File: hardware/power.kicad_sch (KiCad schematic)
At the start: 42 parts, among them J15 Conn_01x02, Q13 DMP3013SFV, Q14 BC817W, U10 FP6151XR-G1, U8 ZTP7193MA

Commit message: clean up
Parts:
- removed Q14: BC817W, Package_TO_SOT_SMD:SOT-323_SC-70, symbol Transistor_BJT:BC817W
- added Q12: AO3400A, Package_TO_SOT_SMD:SOT-23, symbol Transistor_FET:AO3400A
- D3: renamed from D4; LCSC (none) -> C19077535
- renumbered C27 to C14, C36 to C15, C29 to C16, C31 to C17, C37 to C18, C38 to C19, C39 to C20, C33 to C21, C40 to C22, C35 to C23, C41 to C24, D3 to D4, J15 to J14, L3 to L1, Q13 to Q11, R40 to R26, R56 to R27, R44 to R28, R45 to R29, R46 to R30, R57 to R31, R58 to R32, R48 to R33, R59 to R34, R60 to R35, R51 to R36, R52 to R37, R53 to R38, R54 to R39, R55 to R40, TP7 to TP5, U8 to U5, U10 to U6
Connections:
- net GND: now also Q12.2 (S)
- net at R38.2, R39.1: now also Q12.1 (G)
- net at LED1.1 (K): now also Q12.3 (D)
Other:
- note added: "Need to set EN to be >6V"
- note added: "Power Supplies"
- note added: "Reverse Voltage Protection Q11 body diode blocks reverse polarity D2 will clamp V_{GS} to +10V"
- note removed: "Filtering Over Voltage Reverse Voltage"
- note removed: "Make input PMOS larger and include soft start Include large bulk cap for LEDs"
- note removed: "Reverse Voltage Protection Q1 body diode blocks reverse polarity D1 will clamp V_{GS} to +10V"

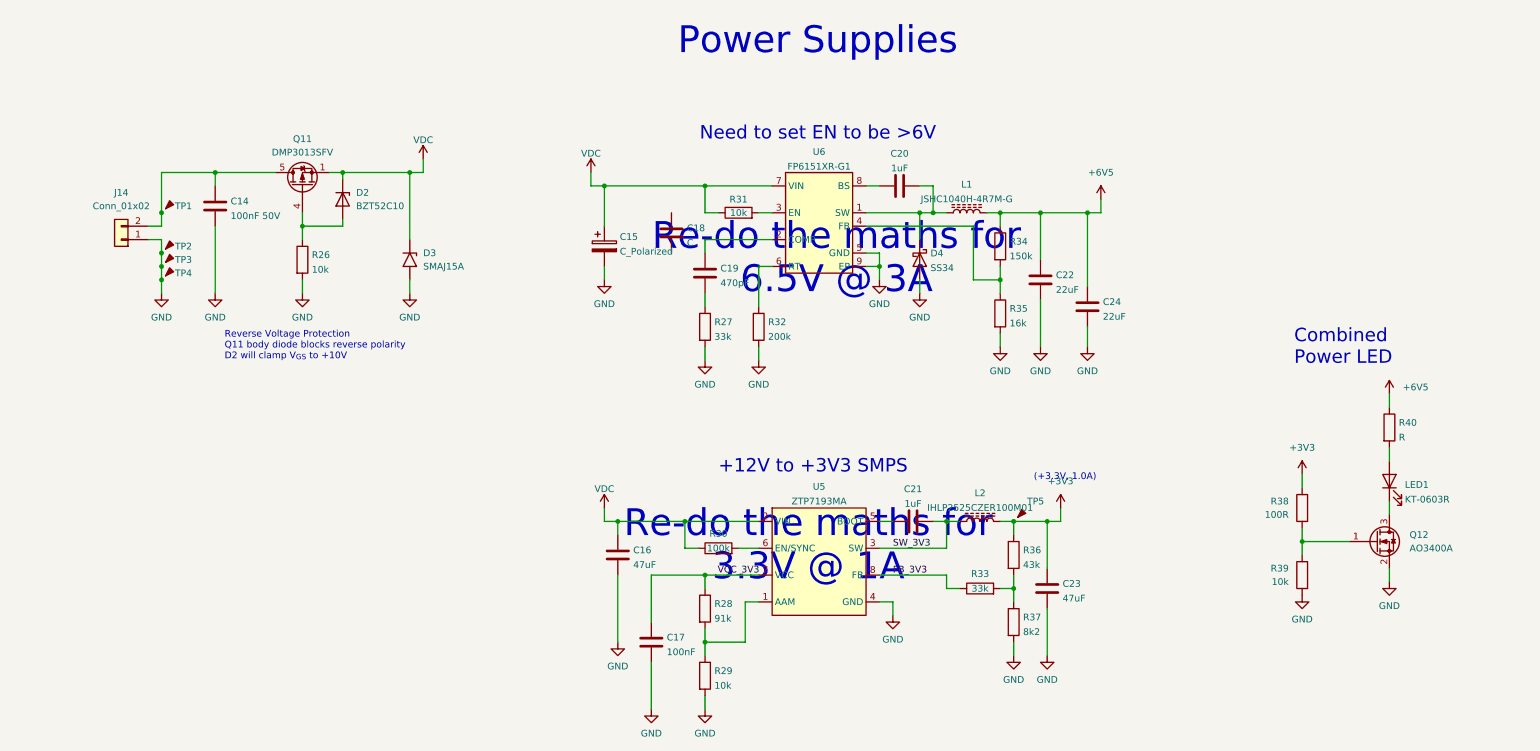
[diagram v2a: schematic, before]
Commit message: updating PSUs
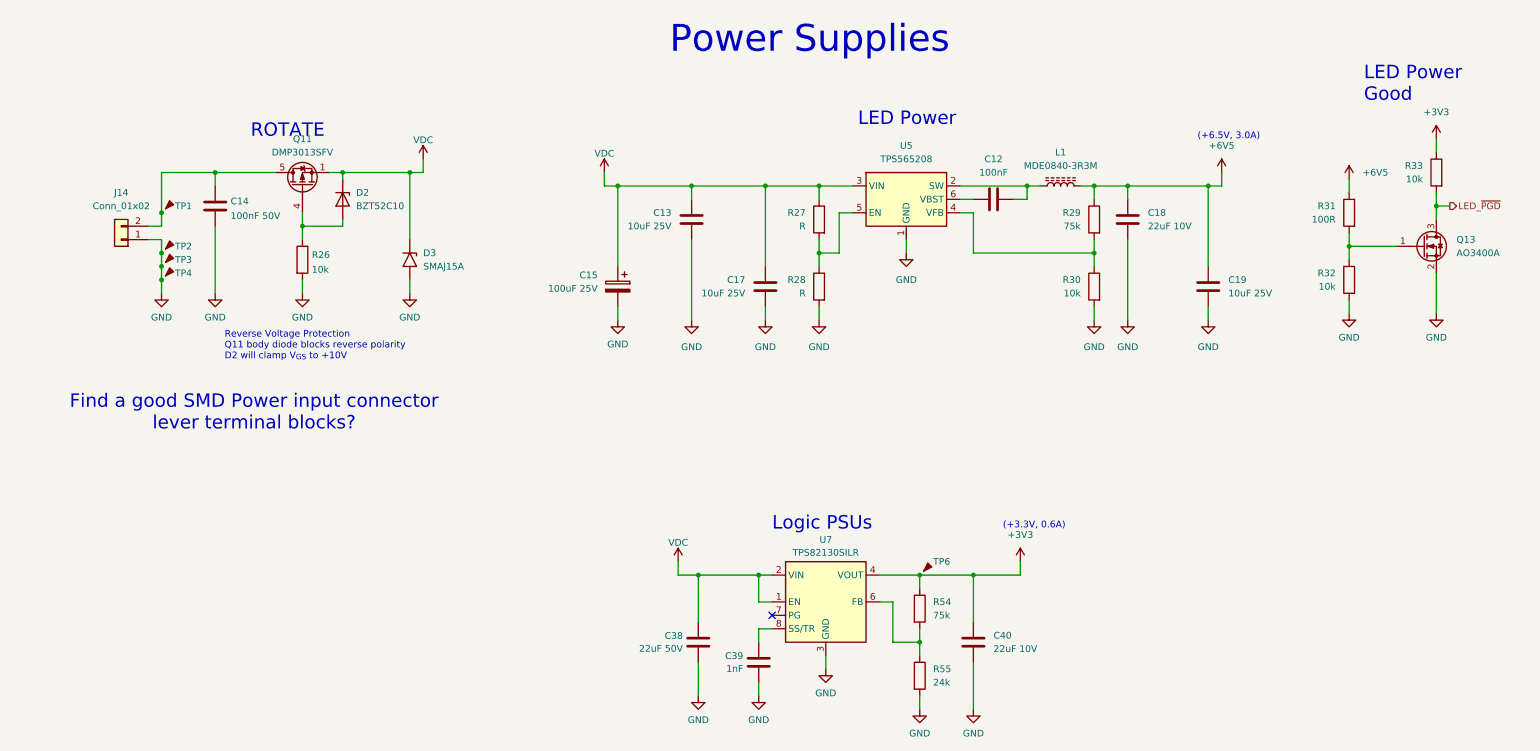
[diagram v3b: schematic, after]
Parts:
- removed C16, C23: 47uF, Capacitor_SMD:C_1210_3225Metric, symbol Device:C
- removed C20, C21: 1uF, Capacitor_SMD:C_0603_1608Metric, symbol Device:C
- removed C22, C24: 22uF, Capacitor_SMD:C_1206_3216Metric, symbol Device:C
- removed D4: SS34, Diode_SMD:D_SMA, symbol Device:D_Schottky
- removed L2: IHLP2525CZER100M01, Inductor_SMD:L_Vishay_IHLP-2525, symbol Device:L_Ferrite
- removed LED1: KT-0603R, LED_SMD:LED_0603_1608Metric, symbol Device:LED
- removed Q12: AO3400A, Package_TO_SOT_SMD:SOT-23, symbol Transistor_FET:AO3400A
- removed R34: 150k, Resistor_SMD:R_0603_1608Metric, symbol Device:R
- removed R35: 16k, Resistor_SMD:R_0603_1608Metric, symbol Device:R
- removed R36: 43k, Resistor_SMD:R_0603_1608Metric, symbol Device:R
- removed R37: 8k2, Resistor_SMD:R_0603_1608Metric, symbol Device:R
- removed R38: 100R, Resistor_SMD:R_0603_1608Metric, symbol Device:R
- removed R39: 10k, Resistor_SMD:R_0603_1608Metric, symbol Device:R
- removed R40: R, Resistor_SMD:R_0603_1608Metric, symbol Device:R
- removed TP5: TestPoint, TestPoint:TestPoint_Pad_D1.5mm, symbol Pinski1_Parts:TestPoint
- removed U5: ZTP7193MA, Package_TO_SOT_SMD:SOT-23-8, symbol Pinski1_Parts:ZTP7193MA
- removed U6: FP6151XR-G1, Package_SO:HSOP-8-1EP_3.9x4.9mm_P1.27mm_EP2.41x3.1mm, symbol Pinski1_Parts:FP6151XR-G1
- added C12: 100nF, Capacitor_SMD:C_0603_1608Metric, symbol Device:C
- added C13: 10uF 25V, Capacitor_SMD:C_0805_2012Metric, symbol Device:C
- added C38: 22uF 50V, Capacitor_SMD:C_1210_3225Metric, symbol Device:C
- added C39: 1nF, Capacitor_SMD:C_0402_1005Metric, symbol Device:C
- added C40: 22uF 10V, Capacitor_SMD:C_0805_2012Metric, symbol Device:C
- added Q13: AO3400A, Package_TO_SOT_SMD:SOT-23, symbol Transistor_FET:AO3400A
- added R54: 75k, Resistor_SMD:R_0603_1608Metric, symbol Device:R
- added R55: 24k, Resistor_SMD:R_0603_1608Metric, symbol Device:R
- added TP6: TestPoint, TestPoint:TestPoint_Pad_D1.5mm, symbol Pinski1_Parts:TestPoint
- added U5: TPS565208, Package_TO_SOT_SMD:SOT-23-6, symbol Regulator_Switching:TPS565208
- added U7: TPS82130SILR, Package_LGA:Texas_SIL0008D_MicroSiP-8-1EP_2.8x3mm_P0.65mm_EP1.1x1.9mm, symbol Regulator_Switching:TPS82130
- C14: LCSC (none) -> C14663
- C15: value C_Polarized -> 100uF 25V
- C17: value 100nF -> 10uF 25V; footprint Capacitor_SMD:C_0603_1608Metric -> Capacitor_SMD:C_0805_2012Metric; LCSC C14663 -> (none); Voltage 50V -> (none)
- C18: value C -> 22uF 10V; footprint Capacitor_SMD:C_1210_3225Metric -> Capacitor_SMD:C_0805_2012Metric
- C19: value 470pF -> 10uF 25V; footprint Capacitor_SMD:C_0603_1608Metric -> Capacitor_SMD:C_0805_2012Metric
- L1: value JSHC1040H-4R7M-G -> MDE0840-3R3M; footprint Inductor_SMD:L_Wuerth_HCI-1040 -> Inductor_SMD:L_Vishay_IHLP-3232; LCSC C334103 -> C2875738
- R26: LCSC C25804 -> C21190
- R27: value 33k -> R
- R28: value 91k -> R; LCSC C23265 -> (none)
- R29: value 10k -> 75k; LCSC C25804 -> (none)
- R30: value 100k -> 10k; LCSC C25803 -> C21190
- R31: value 10k -> 100R; LCSC (none) -> C22775
- R32: value 200k -> 10k; LCSC (none) -> C21190
- R33: value 33k -> 10k; LCSC C4216 -> C21190
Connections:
- net FB_3V3 is gone; now on net +3V3: R33.1
- net +3V3: now also C40.1, R54.1, TP6.1, U7.4 (VOUT), U7.5 (VOUT)
- net +6V5: now also C18.1, C19.1, R29.1, R31.1
- net GND: now also C17.2, C18.2, C19.2, R28.2, R30.2, C13.2, C38.2, C39.2, C40.2, Q13.2 (S), R55.2, U5.1 (GND), U7.3 (GND), U7.9 (GND); no longer C17.1, R27.2, R29.2
- net VDC: now also C17.1, R27.1, C13.1, C38.1, U5.3 (VIN), U7.1 (EN), U7.2 (VIN); no longer R30.1, R31.1
- net LED_~{PGD}: now reaches R33.2
- net LED_~{PGD}: now also Q13.3 (D)
- net at R31.2: now also R32.1, Q13.1 (G)
- net at L1.1: now also C12.2, U5.2 (SW)
- net VCC_3V3: no longer names the net of R28.1
- net VCC_3V3: now also R27.2, U5.5 (EN); no longer C17.2
- new net: R54.2, R55.1, U7.6 (FB)
- new net: R29.2, R30.1, U5.4 (VFB)
- new net: C12.1, U5.6 (VBST)
- new net: C39.1, U7.8 (SS/TR)
- no-connect marks 0 -> 1
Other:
- note added: "(+3.3V, 0.6A)"
- note added: "(+6.5V, 3.0A)"
- note added: "Find a good SMD Power input connector lever terminal blocks?"
- note added: "LED Power"
- note added: "LED Power Good"
- note added: "Logic PSUs"
- note added: "ROTATE"
- note removed: "(+3.3V, 1.0A)"
- note removed: "+12V to +3V3 SMPS"
- note removed: "Combined Power LED"
- note removed: "Need to set EN to be >6V"
- note removed: "Re-do the maths for 3.3V @ 1A"
- note removed: "Re-do the maths for 6.5V @ 3A"
- moved on the sheet: C15

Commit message: some jlc cleanup
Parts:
- removed R27, R28: R, Resistor_SMD:R_0603_1608Metric, symbol Device:R
- C12: LCSC (none) -> C14663
- C13, C17: LCSC (none) -> C15850
- C15: footprint (none) -> Capacitor_SMD:CP_Elec_6.3x7.7; LCSC (none) -> C72477
- C18: LCSC (none) -> C45783
- C19: value 10uF 25V -> 22uF 10V; LCSC (none) -> C45783
- C39: footprint Capacitor_SMD:C_0402_1005Metric -> Capacitor_SMD:C_0603_1608Metric; LCSC C1523 -> C1588
- C40: LCSC C96123 -> C45783
- J14: footprint Connector_Phoenix_MSTB:PhoenixContact_MSTBVA_2,5_2-G-5,08_1x02_P5.08mm_Vertical -> (none); LCSC (none) -> C7467028
- R26, R30, R32, R33: LCSC C21190 -> C25804
- R29, R54: LCSC (none) -> C23242
- R55: LCSC (none) -> C23352
- renumbered Q13 to Q11, Q11 to Q12
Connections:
- net VDC: now also U5.5 (EN)
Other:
- note added: "Do we really need a 22uF 50V 1210 MLCC cap?"
- note added: "EMC ferrites /CMC?"
- moved on the sheet: C12, C13, C14, C15, C17, C18, C38, C39, C40, D2, D3, J14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

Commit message: tweaking lcsc part numbers
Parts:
- removed C38: 22uF 50V, Capacitor_SMD:C_1210_3225Metric, symbol Device:C
- added C20, C21, C22: 10uF 25V, Capacitor_SMD:C_0805_2012Metric, symbol Device:C
- Q12: Rotation_offset (none) -> -90
- U7: value TPS82130SILR -> TPS82140SILR; LCSC C473914 -> C544385; Rotation_offset (none) -> 180
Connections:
- net GND: now also C20.2, C21.2, C22.2
- net VDC: now also C20.1, C21.1, C22.1
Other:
- note added: "LED Buck"
- note added: "Logic Buck"
- note added: "OUT OF STOCK!"
- note added: "Reverse Voltage Protection Q12 body diode blocks reverse polarity D2 will clamp V_{GS} to +10V"
- note added: "Standard Assy only?!"
- note removed: "Do we really need a 22uF 50V 1210 MLCC cap?"
- note removed: "LED Power"
- note removed: "Logic PSUs"
- note removed: "Reverse Voltage Protection Q11 body diode blocks reverse polarity D2 will clamp V_{GS} to +10V"

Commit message: general schematic and PCB clean
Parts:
- C15: LCSC C72477 -> C267469
- J14: footprint (none) -> TerminalBlock_WAGO:TerminalBlock_WAGO_2601-3102_1x02_P3.50mm_Vertical
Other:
- note added: "ROTATE FIX"
- note added: "V_{R} = 15.0 V_{BR min} = 16.70 V_{BR max} = 18.50 V_{C} = 24.4"
- note removed: "ROTATE"
- note removed: "Standard Assy only?!"
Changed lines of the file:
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@@
 		)
 	)
-	(text "Standard Assy only?!"
+	(text "V_{R} = 15.0\nV_{BR min} = 16.70\nV_{BR max} = 18.50\nV_{C} = 24.4"
 		(exclude_from_sim no)
-		(at 106.172 75.692 0)
+		(at 82.804 109.474 0)
 		(effects
 			(font
-				(size 2.54 2.54)
-				(color 255 0 0 1)
+				(size 1.27 1.27)
 			)
+			(justify left top)
 		)
 	)
@@
 	(text "Find a good SMD Power input connector\nlever terminal blocks?"
 		(exclude_from_sim no)
-		(at 56.134 132.334 0)
+		(at 56.896 136.906 0)
 		(effects
 			(font
@@
 	(text "EMC ferrites /CMC?"
 		(exclude_from_sim no)
-		(at 58.42 140.97 0)
+		(at 59.182 145.542 0)
 		(effects
 			(font
@@
 		)
 	)
-	(text "ROTATE"
+	(text "ROTATE\nFIX"
 		(exclude_from_sim no)
 		(at 24.638 101.346 0)
@@
 			)
 		)
-		(property "Footprint" ""
+		(property "Footprint" "TerminalBlock_WAGO:TerminalBlock_WAGO_2601-3102_1x02_P3.50mm_Vertical"
 			(at 25.4 102.87 0)
 			(effects
@@
 			)
 		)
-		(property "LCSC" "C72477"
+		(property "LCSC" "C267469"
 			(at 111.76 72.39 0)
 			(effects

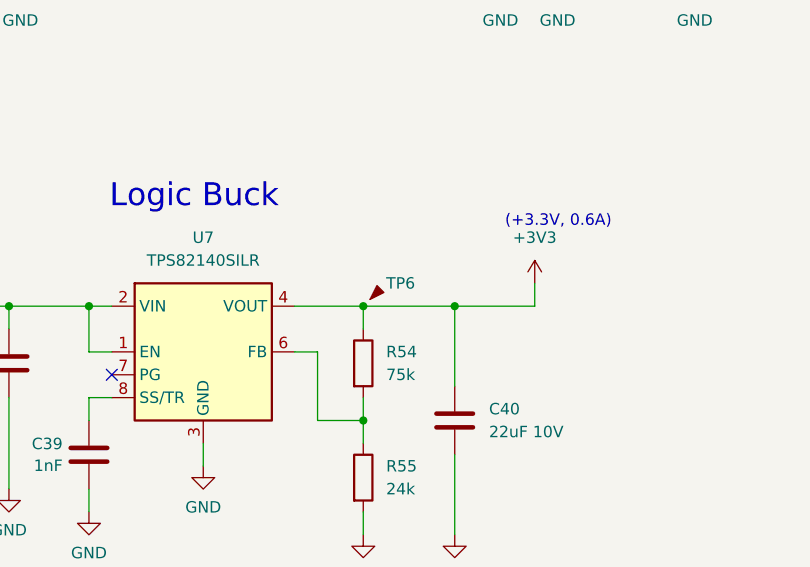
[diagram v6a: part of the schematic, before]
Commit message: sorting button and LED
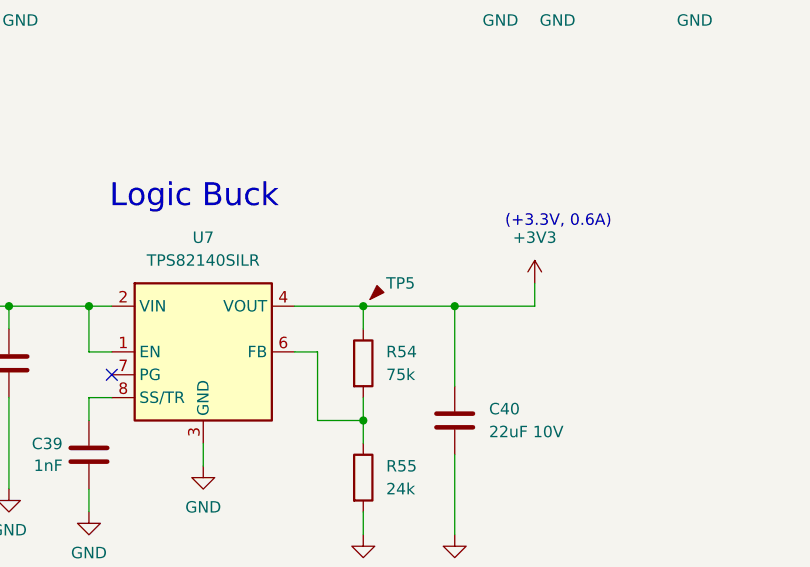
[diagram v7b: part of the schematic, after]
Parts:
- C15: Rotation Offset (none) -> 180
- Q12: Rotation Offset (none) -> -90; Rotation_offset -90 -> (none)
- TP1, TP2, TP3, TP4: now left out of the parts list
- TP5: renamed from TP6; now left out of the parts list
- U7: Rotation Offset (none) -> 180; Rotation_offset 180 -> (none)

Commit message: starting layout
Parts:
- added TP6, TP7: TestPoint, TestPoint:TestPoint_Pad_D1.5mm, symbol Pinski1_Parts:TestPoint
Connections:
- net +6V5: now also TP7.1
- net VDC: now also TP6.1
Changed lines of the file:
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@@
+	)
+	(symbol
+		(lib_id "Pinski1_Parts:TestPoint")
+		(at 199.39 53.34 0)
+		(unit 1)
+		(exclude_from_sim no)
+		(in_bom no)
+		(on_board yes)
+		(dnp no)
+		(property "Reference" "TP7"
+			(at 201.93 50.8 0)
+			(effects
+				(font
+					(size 1.27 1.27)
+				)
+				(justify left)
+			)
+		)
+		(property "Value" "TestPoint"
+			(at 201.422 51.308 0)
+			(effects
+				(font
+					(size 1.27 1.27)
+				)
+				(justify left bottom)
+				(hide yes)
+			)
+		)
+		(property "Footprint" "TestPoint:TestPoint_Pad_D1.5mm"
+			(at 199.39 53.34 0)
+			(effects
+				(font
+					(size 1.27 1.27)
+				)
+				(hide yes)
+			)
+		)
+		(property "Datasheet" "~"
+			(at 199.39 53.34 0)
+			(effects
+				(font
+					(size 1.27 1.27)
+				)
+				(hide yes)
+			)
+		)
+		(property "Description" ""
+			(at 199.39 53.34 0)
+			(effects
+				(font
+					(size 1.27 1.27)
+				)
+			)
+		)
+		(property "LCSC" "~"
+			(at 199.39 53.34 0)
+			(effects
+				(font
+					(size 1.27 1.27)
+				)
+				(hide yes)
+			)
+		)
+		(pin "1"
+		)
+		(instances
+			(project "emf_beacon"
+				(path "/0654b480-d862-4382-88d5-1ac411bf5574/47676e1e-c686-4542-ba08-5a0ba3501dcc"
+					(reference "TP7")
+					(unit 1)
+				)
+			)
+		)
 	)
 	(symbol
@@
 					(unit 1)
 				)
+			)
+		)
+	)
+	(symbol
+		(lib_id "Pinski1_Parts:TestPoint")
+		(at 67.31 90.17 0)
+		(unit 1)
+		(exclude_from_sim no)
+		(in_bom no)
+		(on_board yes)
+		(dnp no)
+		(property "Reference" "TP6"
+			(at 69.85 88.9 0)
+			(effects
+				(font
+					(size 1.27 1.27)
+				)
+				(justify left)
+			)
+		)
+		(property "Value" "TestPoint"
+			(at 69.342 88.138 0)
+			(effects
+				(font
+					(size 1.27 1.27)
+				)
+				(justify left bottom)
+				(hide yes)
+			)
+		)
+		(property "Footprint" "TestPoint:TestPoint_Pad_D1.5mm"
+			(at 67.31 90.17 0)
+			(effects
+				(font
+					(size 1.27 1.27)
+				)
+				(hide yes)
+			)
+		)
+		(property "Datasheet" "~"
+			(at 67.31 90.17 0)
+			(effects
+				(font
+					(size 1.27 1.27)
+				)
+				(hide yes)
+			)
+		)
+		(property "Description" ""
+			(at 67.31 90.17 0)
+			(effects
+				(font
+					(size 1.27 1.27)
+				)
+			)
+		)
+		(property "LCSC" "~"
+			(at 67.31 90.17 0)
+			(effects
+				(font
+					(size 1.27 1.27)
+				)
+				(hide yes)
+			)
+		)
+		(property "MFR" ""
+			(at 67.31 90.17 0)
+			(effects
+				(font
+					(size 1.27 1.27)
+				)
+				(hide yes)
+			)
+		)
+		(property "MPN" ""
+			(at 67.31 90.17 0)
+			(effects
+				(font
+					(size 1.27 1.27)
+				)
+				(hide yes)
+			)
+		)
+		(pin "1"
+		)
+		(instances
+			(project "emf_beacon"
+				(path "/0654b480-d862-4382-88d5-1ac411bf5574/47676e1e-c686-4542-ba08-5a0ba3501dcc"
+					(reference "TP6")
+					(unit 1)
+				)
